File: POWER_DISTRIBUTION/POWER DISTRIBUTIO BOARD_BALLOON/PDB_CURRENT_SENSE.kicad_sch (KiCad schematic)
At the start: 3 parts, among them IC8 INA232AIDDFR

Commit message: POWER BOARD LAYOUT COMPLETE
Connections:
- net VCC_BALANCE is gone; now on net +3.3V: C47.2
- net VBAT+ renamed VBAT_Fused

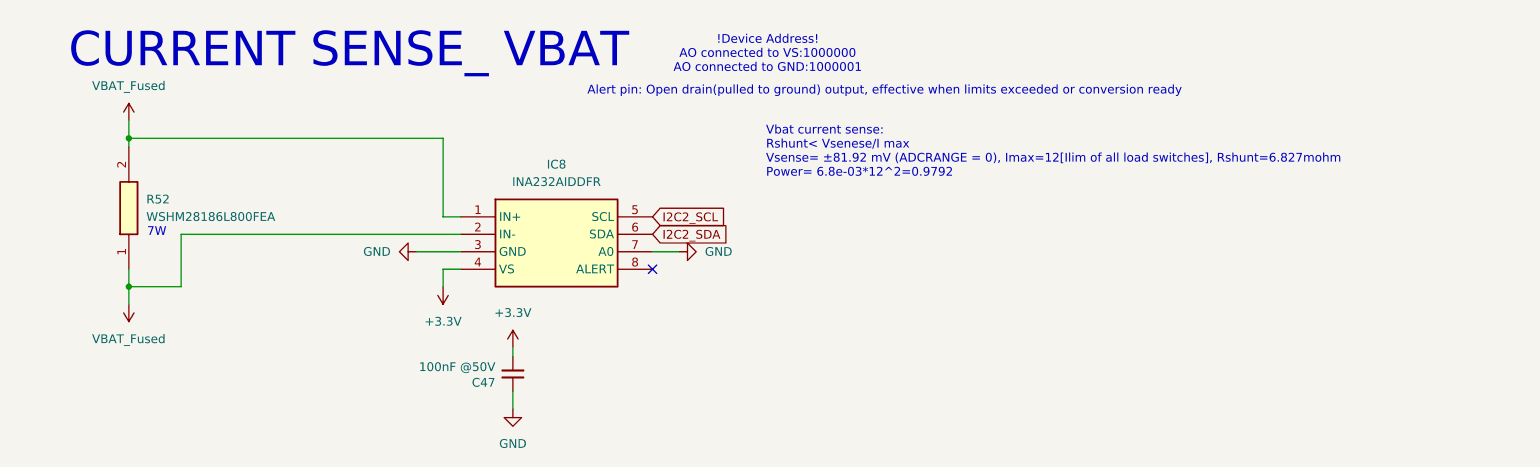
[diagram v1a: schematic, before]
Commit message: almost finished wiring
btw for the i2c bus idk if it was meant to be SCL instead of SDL , there is alr an SDA line but i assume so
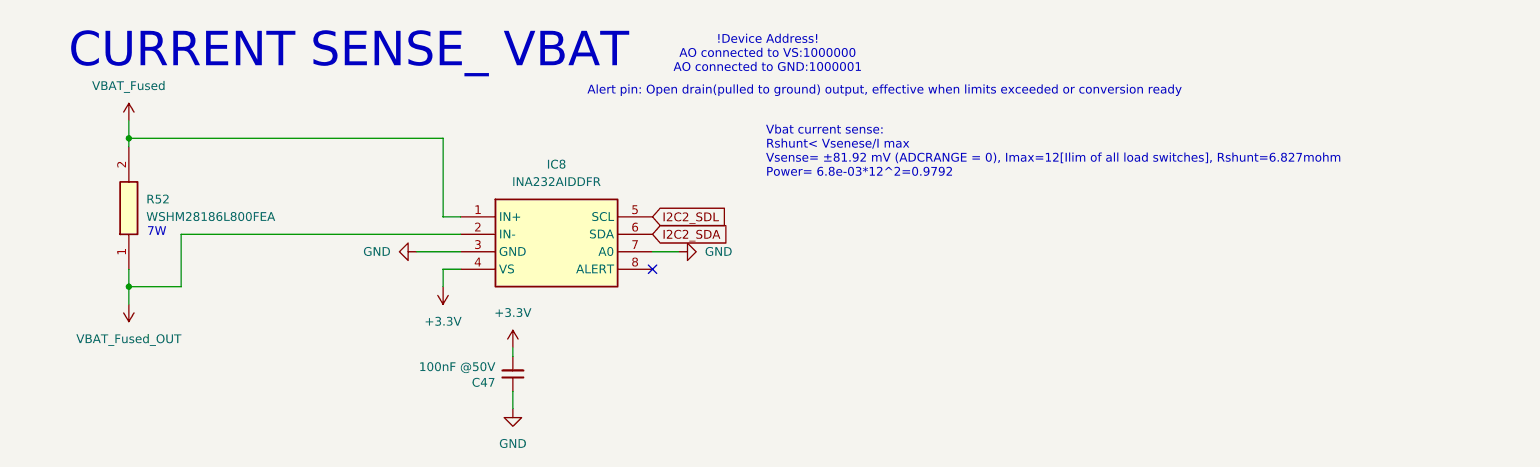
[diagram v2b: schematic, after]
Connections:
- net VBAT_Fused: no longer IC8.2 (IN-), R52.1
- net I2C2_SCL renamed I2C2_SDL
- new net VBAT_Fused_OUT: IC8.2 (IN-), R52.1
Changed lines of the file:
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@@
 		)
 	)
-	(global_label "I2C2_SCL"
+	(global_label "I2C2_SDL"
 		(shape input)
 		(at 130.81 88.9 0)
@@
 			)
 		)
-		(property "Value" "VBAT_Fused"
+		(property "Value" "VBAT_Fused_OUT"
 			(at 54.61 106.68 0)
 			(effects
